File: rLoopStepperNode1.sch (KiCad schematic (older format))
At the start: 29 parts

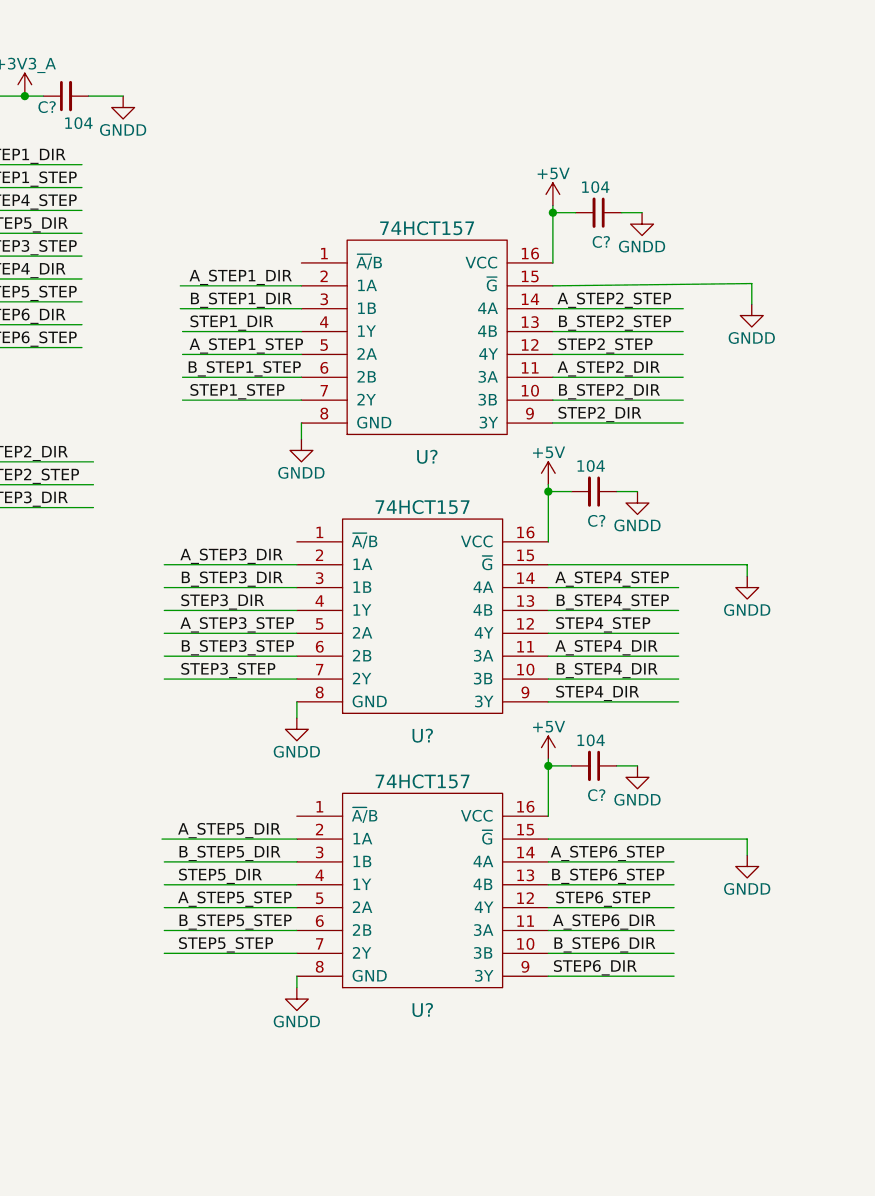
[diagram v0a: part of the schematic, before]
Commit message: Move Multiplexers
Moved multiplexers into their own schematic sheet in preparation of
making the interfaces to the G210x drive controllers.
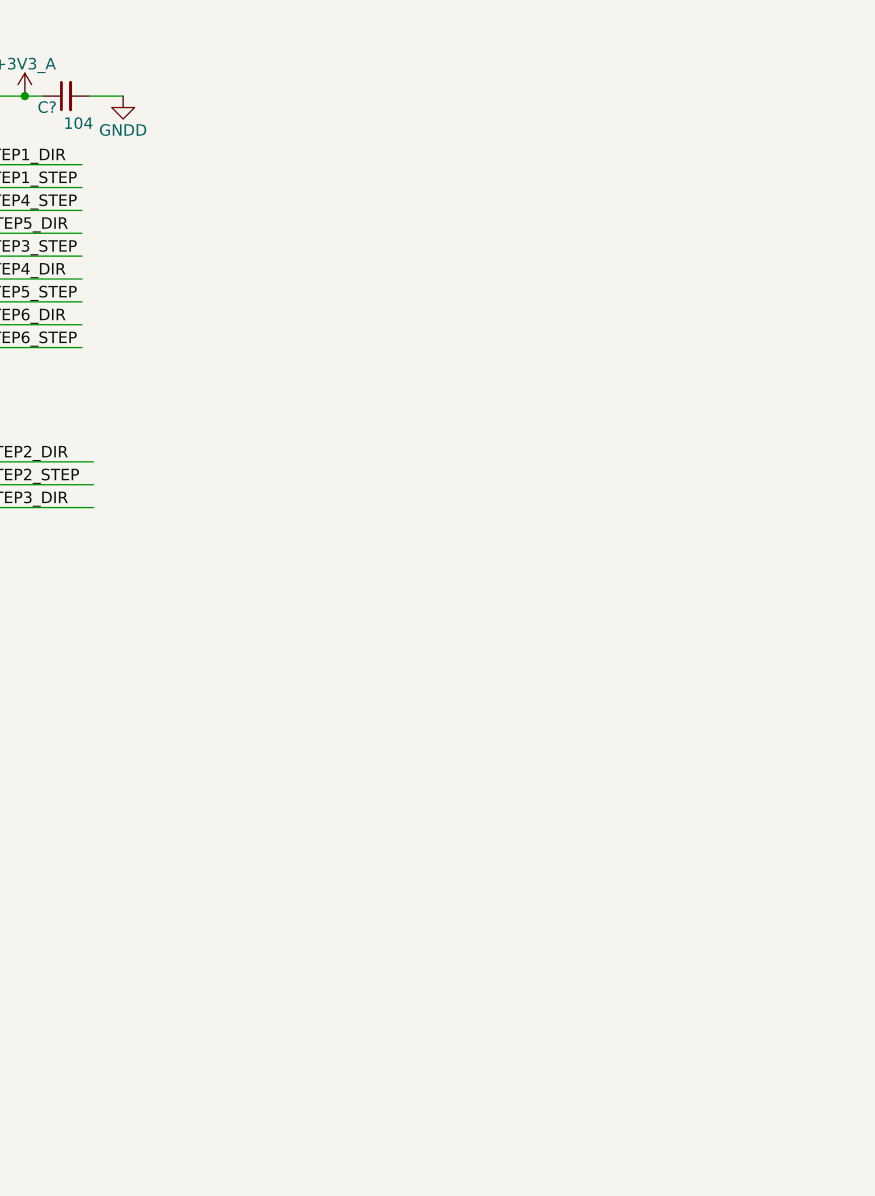
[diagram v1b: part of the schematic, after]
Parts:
- removed C? (x3): 104, symbol C_Small
- removed U? (x3): 74HCT157, symbol 74HCT157
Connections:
- net labels removed: +5V, STEP1_DIR, STEP1_STEP, STEP2_DIR, STEP2_STEP, STEP3_DIR, STEP3_STEP, STEP4_DIR, STEP4_STEP, STEP5_DIR, STEP5_STEP, STEP6_DIR, STEP6_STEP
- wire segments 169 -> 115

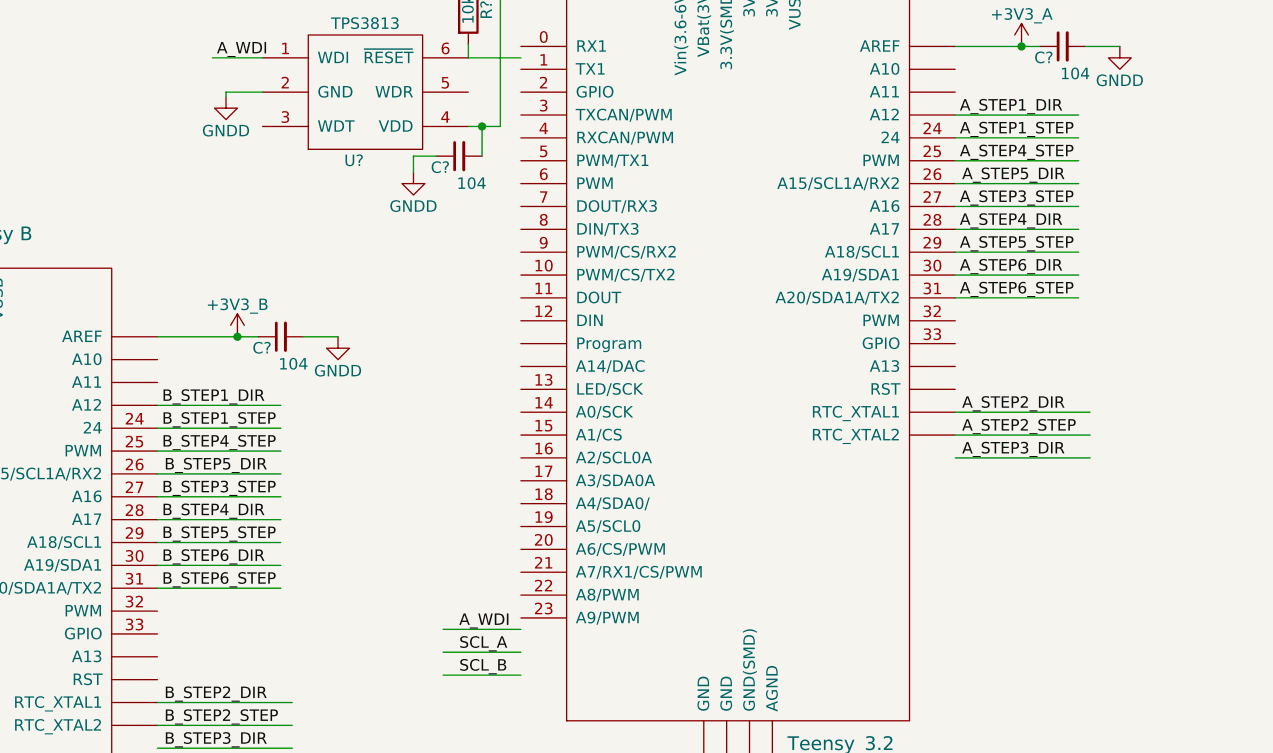
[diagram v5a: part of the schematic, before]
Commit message: Remove Gimbal Functions
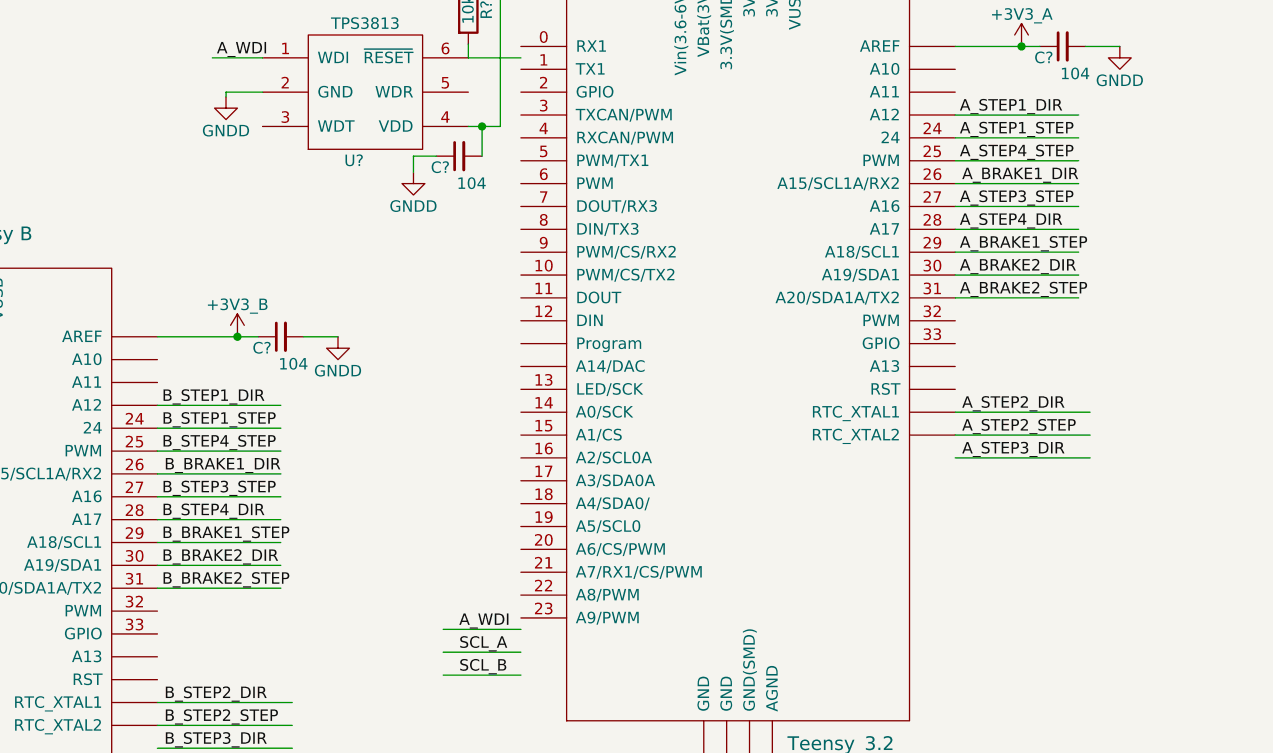
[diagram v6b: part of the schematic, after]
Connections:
- net labels added: A_BRAKE1_DIR, A_BRAKE1_STEP, A_BRAKE2_DIR, A_BRAKE2_STEP, B_BRAKE1_DIR, B_BRAKE1_STEP, B_BRAKE2_DIR, B_BRAKE2_STEP
- net labels removed: A_STEP5_DIR, A_STEP5_STEP, A_STEP6_DIR, A_STEP6_STEP, B_STEP5_DIR, B_STEP5_STEP, B_STEP6_DIR, B_STEP6_STEP
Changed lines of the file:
@@
 A_STEP4_STEP
 Text Label 7570 2250 0    50   ~ 0
-A_STEP5_DIR
+A_BRAKE1_DIR
 Text Label 7560 2550 0    50   ~ 0
-A_STEP5_STEP
+A_BRAKE1_STEP
 Text Label 7560 2650 0    50   ~ 0
-A_STEP6_DIR
+A_BRAKE2_DIR
 Text Label 7560 2750 0    50   ~ 0
-A_STEP6_STEP
+A_BRAKE2_STEP
 $Comp
 L Teensy_3.2 U?
@@
 B_STEP4_STEP
 Text Label 4080 3520 0    50   ~ 0
-B_STEP5_DIR
+B_BRAKE1_DIR
 Text Label 4070 3820 0    50   ~ 0
-B_STEP5_STEP
+B_BRAKE1_STEP
 Text Label 4070 3920 0    50   ~ 0
-B_STEP6_DIR
+B_BRAKE2_DIR
 Text Label 4070 4020 0    50   ~ 0
-B_STEP6_STEP
+B_BRAKE2_STEP
 $Comp
 L TPS3813 U?
